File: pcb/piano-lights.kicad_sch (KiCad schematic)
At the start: 35 parts, among them J1 FTDI RS232, J2 USB_B_Micro, J3 LED Strip, J4 AVR-ISP-6, J5 MIDI IN, J6 MIDI THRU, J7 MIDI Coupler Out, J8 MIDI Coupler In, SW2 Reset, U1 ATmega328P-P, U2 H11L1, U3 74AHC1G125, Y1 16MHz

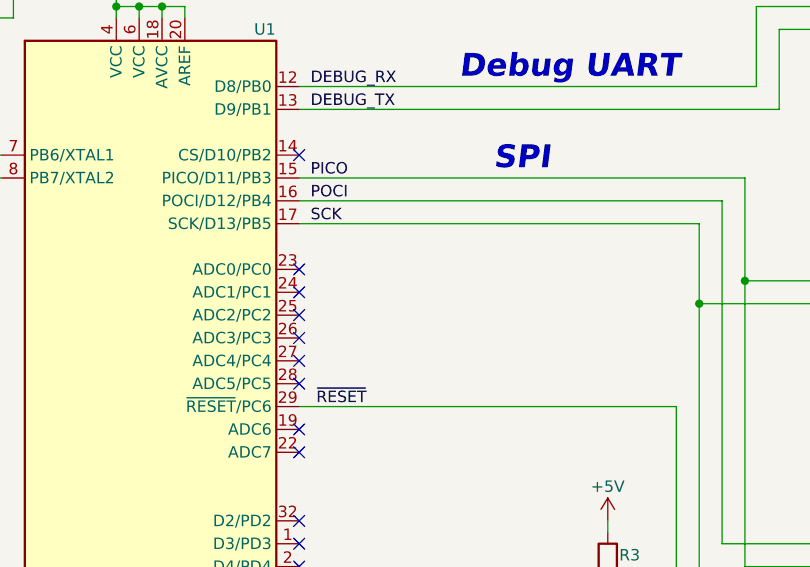
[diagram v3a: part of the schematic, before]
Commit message: Add the button back, but on a different pin. Start cleaning up silkscreen
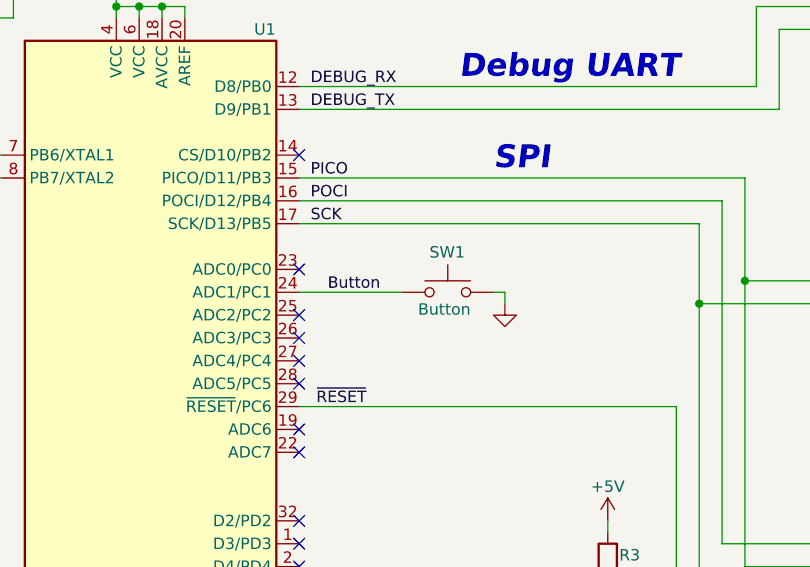
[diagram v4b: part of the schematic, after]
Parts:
- added SW1: Button, Button_Switch_THT:SW_PUSH_6mm_H5mm, symbol Switch:SW_Push
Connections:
- net GND: now also SW1.2
- net Button: now reaches U1.24 (ADC1/PC1)
- net Button: now also SW1.1
- no-connect marks 30 -> 29
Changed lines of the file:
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@@
   (no_connect (at 130.81 63.5))
   (no_connect (at 130.81 101.6))
-  (no_connect (at 130.81 66.04))
   (no_connect (at 130.81 68.58))
   (no_connect (at 130.81 71.12))
@@
     (stroke (width 0) (type default) (color 0 0 0 0))
   )
+  (wire (pts (xy 130.81 66.04) (xy 142.24 66.04))
+    (stroke (width 0) (type default) (color 0 0 0 0))
+  )
   (wire (pts (xy 44.45 50.8) (xy 45.72 50.8))
     (stroke (width 0) (type default) (color 0 0 0 0))
@@
     (stroke (width 0) (type default) (color 0 0 0 0))
   )
+  (wire (pts (xy 153.67 66.04) (xy 153.67 67.31))
+    (stroke (width 0) (type default) (color 0 0 0 0))
+  )
   (polyline (pts (xy 191.77 48.26) (xy 191.77 74.93))
     (stroke (width 0) (type default) (color 0 0 0 0))
@@
   )
   (wire (pts (xy 220.98 154.94) (xy 220.98 147.066))
+    (stroke (width 0) (type default) (color 0 0 0 0))
+  )
+  (wire (pts (xy 152.4 66.04) (xy 153.67 66.04))
     (stroke (width 0) (type default) (color 0 0 0 0))
   )
@@
   )
   (label "MCOUP_DATA" (at 232.41 157.48 0)
+    (effects (font (size 1.27 1.27)) (justify left bottom))
+  )
+  (label "Button" (at 133.985 66.04 0)
     (effects (font (size 1.27 1.27)) (justify left bottom))
   )
@@
     (pin "9")
   )
+  (symbol (lib_id "Switch:SW_Push") (at 147.32 66.04 0) (unit 1)
+    (in_bom yes) (on_board yes)
+    (property "Reference" "SW1" (id 0) (at 149.225 61.595 0)
+      (effects (font (size 1.27 1.27)) (justify right))
+    )
+    (property "Value" "Button" (id 1) (at 149.86 67.945 0)
+      (effects (font (size 1.27 1.27)) (justify right))
+    )
+    (property "Footprint" "Button_Switch_THT:SW_PUSH_6mm_H5mm" (id 2) (at 147.32 60.96 0)
+      (effects (font (size 1.27 1.27)) hide)
+    )
+    (property "Datasheet" "~" (id 3) (at 147.32 60.96 0)
+      (effects (font (size 1.27 1.27)) hide)
+    )
+    (pin "1")
+    (pin "2")
+  )
   (symbol (lib_id "power:+5V") (at 199.39 54.61 0) (unit 1)
     (in_bom yes) (on_board yes)
@@
     )
     (property "Datasheet" "" (id 3) (at 110.49 20.32 0)
+      (effects (font (size 1.27 1.27)) hide)
+    )
+    (pin "1")
+  )
+  (symbol (lib_id "power:GND") (at 153.67 67.31 0) (mirror y) (unit 1)
+    (in_bom yes) (on_board yes) (fields_autoplaced)
+    (property "Reference" "#PWR?" (id 0) (at 153.67 73.66 0)
+      (effects (font (size 1.27 1.27)) hide)
+    )
+    (property "Value" "GND" (id 1) (at 153.67 72.39 0)
+      (effects (font (size 1.27 1.27)) hide)
+    )
+    (property "Footprint" "" (id 2) (at 153.67 67.31 0)
+      (effects (font (size 1.27 1.27)) hide)
+    )
+    (property "Datasheet" "" (id 3) (at 153.67 67.31 0)
       (effects (font (size 1.27 1.27)) hide)
     )
@@
       (reference "#PWR028") (unit 1) (value "GND") (footprint "")
     )
+    (path "/a6dd2b86-9adf-4b95-abc2-e26c3254edb0"
+      (reference "#PWR?") (unit 1) (value "GND") (footprint "")
+    )
     (path "/9521ebc8-4618-4f81-a564-0a20e7137d6b"
       (reference "C1") (unit 1) (value "100n") (footprint "Capacitor_SMD:C_0603_1608Metric_Pad1.08x0.95mm_HandSolder")
@@
       (reference "R6") (unit 1) (value "220") (footprint "Resistor_SMD:R_0603_1608Metric_Pad0.98x0.95mm_HandSolder")
     )
+    (path "/3da00856-5831-42f7-ab8b-b66876dbd199"
+      (reference "SW1") (unit 1) (value "Button") (footprint "Button_Switch_THT:SW_PUSH_6mm_H5mm")
+    )
     (path "/95e292a9-d533-4e45-ad33-fbfe25b833db"

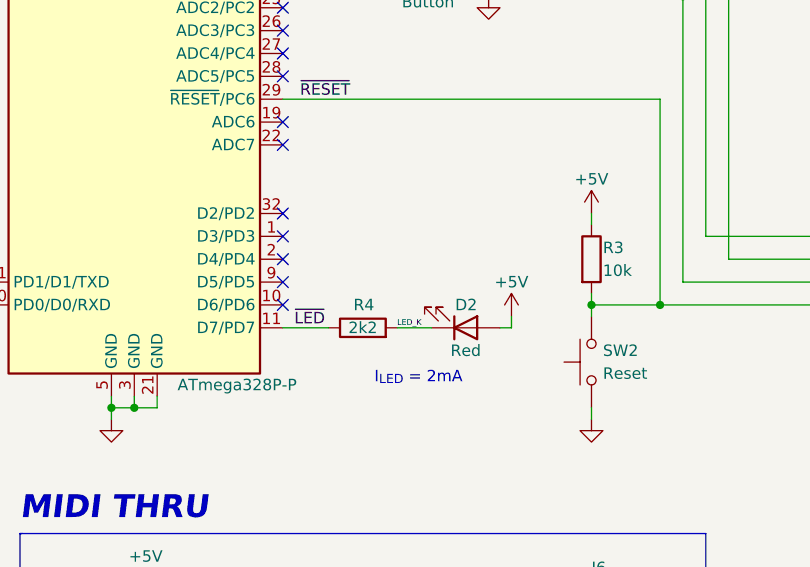
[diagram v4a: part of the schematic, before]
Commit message: Move /LED to Pin 1 for easier PCB routing
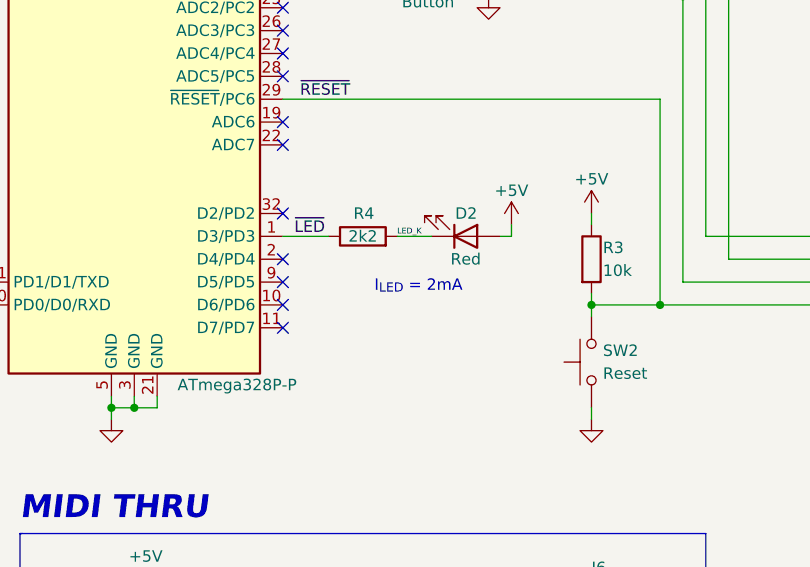
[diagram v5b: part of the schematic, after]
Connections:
- net ~{LED}: now also U1.1 (D3/PD3); no longer U1.11 (D7/PD7)
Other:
- moved on the sheet: D2, R4
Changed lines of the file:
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@@
   (no_connect (at 223.52 144.526))
   (no_connect (at 97.79 99.06))
+  (no_connect (at 130.81 104.14))
   (no_connect (at 130.81 91.44))
   (no_connect (at 130.81 81.28))
@@
   (no_connect (at 130.81 73.66))
   (no_connect (at 130.81 76.2))
-  (no_connect (at 130.81 93.98))
   (no_connect (at 130.81 96.52))
   (no_connect (at 130.81 99.06))
@@
     (stroke (width 0) (type default) (color 0 0 0 0))
   )
-  (wire (pts (xy 130.81 104.14) (xy 135.89 104.14))
+  (wire (pts (xy 130.81 93.98) (xy 135.89 93.98))
     (stroke (width 0) (type default) (color 0 0 0 0))
   )
@@
     (stroke (width 0) (type default) (color 0 0 0 0))
   )
-  (wire (pts (xy 154.94 104.14) (xy 156.21 104.14))
+  (wire (pts (xy 154.94 93.98) (xy 156.21 93.98))
     (stroke (width 0) (type default) (color 0 0 0 0))
   )
@@
     (stroke (width 0) (type default) (color 0 0 0 0))
   )
-  (wire (pts (xy 156.21 104.14) (xy 156.21 102.87))
+  (wire (pts (xy 156.21 93.98) (xy 156.21 92.71))
     (stroke (width 0) (type default) (color 0 0 0 0))
   )
@@
     (stroke (width 0) (type default) (color 0 0 0 0))
   )
-  (wire (pts (xy 143.51 104.14) (xy 147.32 104.14))
+  (wire (pts (xy 143.51 93.98) (xy 147.32 93.98))
     (stroke (width 0) (type default) (color 0 0 0 0))
   )
@@
     (effects (font (size 1.27 1.27)) (justify left bottom))
   )
-  (text "I_{LED} = 2mA" (at 140.97 110.49 0)
+  (text "I_{LED} = 2mA" (at 140.97 100.33 0)
     (effects (font (size 1.27 1.27)) (justify left bottom))
   )
@@
     (effects (font (size 1.27 1.27)) (justify right bottom))
   )
-  (label "LED_K" (at 143.51 104.14 0)
+  (label "LED_K" (at 143.51 93.98 0)
     (effects (font (size 0.635 0.635)) (justify left bottom))
   )
@@
     (effects (font (size 1.27 1.27)) (justify left bottom))
   )
-  (label "~{LED}" (at 132.08 104.14 0)
+  (label "~{LED}" (at 132.08 93.98 0)
     (effects (font (size 1.27 1.27)) (justify left bottom))
   )
@@
     (pin "1")
   )
-  (symbol (lib_id "power:+5V") (at 156.21 102.87 0) (unit 1)
-    (in_bom yes) (on_board yes)
-    (property "Reference" "#PWR017" (id 0) (at 156.21 106.68 0)
-      (effects (font (size 1.27 1.27)) hide)
-    )
-    (property "Value" "+5V" (id 1) (at 156.21 99.06 0))
-    (property "Footprint" "" (id 2) (at 156.21 102.87 0)
-      (effects (font (size 1.27 1.27)) hide)
-    )
-    (property "Datasheet" "" (id 3) (at 156.21 102.87 0)
+  (symbol (lib_id "power:+5V") (at 156.21 92.71 0) (unit 1)
+    (in_bom yes) (on_board yes)
+    (property "Reference" "#PWR017" (id 0) (at 156.21 96.52 0)
+      (effects (font (size 1.27 1.27)) hide)
+    )
+    (property "Value" "+5V" (id 1) (at 156.21 88.9 0))
+    (property "Footprint" "" (id 2) (at 156.21 92.71 0)
+      (effects (font (size 1.27 1.27)) hide)
+    )
+    (property "Datasheet" "" (id 3) (at 156.21 92.71 0)
       (effects (font (size 1.27 1.27)) hide)
     )
@@
   (symbol (lib_id "power:GND") (at 153.67 67.31 0) (mirror y) (unit 1)
     (in_bom yes) (on_board yes) (fields_autoplaced)
-    (property "Reference" "#PWR?" (id 0) (at 153.67 73.66 0)
+    (property "Reference" "#PWR0101" (id 0) (at 153.67 73.66 0)
       (effects (font (size 1.27 1.27)) hide)
     )
@@
     (pin "SH")
   )
-  (symbol (lib_id "Device:LED") (at 151.13 104.14 0) (mirror x) (unit 1)
-    (in_bom yes) (on_board yes)
-    (property "Reference" "D2" (id 0) (at 152.4 101.6 0)
+  (symbol (lib_id "Device:LED") (at 151.13 93.98 0) (mirror x) (unit 1)
+    (in_bom yes) (on_board yes)
+    (property "Reference" "D2" (id 0) (at 152.4 91.44 0)
       (effects (font (size 1.27 1.27)) (justify right))
     )
-    (property "Value" "Red" (id 1) (at 151.13 106.68 0))
-    (property "Footprint" "LED_THT:LED_D3.0mm" (id 2) (at 151.13 104.14 0)
-      (effects (font (size 1.27 1.27)) hide)
-    )
-    (property "Datasheet" "~" (id 3) (at 151.13 104.14 0)
+    (property "Value" "Red" (id 1) (at 151.13 96.52 0))
+    (property "Footprint" "LED_THT:LED_D3.0mm" (id 2) (at 151.13 93.98 0)
+      (effects (font (size 1.27 1.27)) hide)
+    )
+    (property "Datasheet" "~" (id 3) (at 151.13 93.98 0)
       (effects (font (size 1.27 1.27)) hide)
     )
@@
     )
   )
-  (symbol (lib_id "Device:R") (at 139.7 104.14 90) (unit 1)
-    (in_bom yes) (on_board yes)
-    (property "Reference" "R4" (id 0) (at 140.97 101.6 90)
+  (symbol (lib_id "Device:R") (at 139.7 93.98 90) (unit 1)
+    (in_bom yes) (on_board yes)
+    (property "Reference" "R4" (id 0) (at 140.97 91.44 90)
       (effects (font (size 1.27 1.27)) (justify left))
     )
-    (property "Value" "2k2" (id 1) (at 139.7 104.14 90))
-    (property "Footprint" "Resistor_SMD:R_0603_1608Metric_Pad0.98x0.95mm_HandSolder" (id 2) (at 139.7 105.918 90)
-      (effects (font (size 1.27 1.27)) hide)
-    )
-    (property "Datasheet" "~" (id 3) (at 139.7 104.14 0)
+    (property "Value" "2k2" (id 1) (at 139.7 93.98 90))
+    (property "Footprint" "Resistor_SMD:R_0603_1608Metric_Pad0.98x0.95mm_HandSolder" (id 2) (at 139.7 95.758 90)
+      (effects (font (size 1.27 1.27)) hide)
+    )
+    (property "Datasheet" "~" (id 3) (at 139.7 93.98 0)
       (effects (font (size 1.27 1.27)) hide)
     )
@@
     )
     (path "/a6dd2b86-9adf-4b95-abc2-e26c3254edb0"
-      (reference "#PWR?") (unit 1) (value "GND") (footprint "")
+      (reference "#PWR0101") (unit 1) (value "GND") (footprint "")
     )
     (path "/9521ebc8-4618-4f81-a564-0a20e7137d6b"

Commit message: Start adding mfr, part, and vendor to schematic
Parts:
- D2: Mfr (none) -> Würth Elektronik; Part No (none) -> 151031SS04000; Vendor (none) -> https://www.digikey.com/en/products/detail/würth-elektronik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
- J2: Mfr (none) -> Würth Elektronik; Part No (none) -> 629105150521; Vendor (none) -> https://www.digikey.com/en/products/detail/würth-elektronik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
- U2: Mrf (none) -> onsemi; Part No. (none) -> H11L1M; Vendor (none) -> https://www.digikey.com/en/products/detail/onsemi/H11L1M/28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
- U3: Mfr (none) -> Nexperia USA Inc.; Part No (none) -> 74AHC1G125GV,125; Vendor (none) -> https://www.digikey.com/en/products/detail/nexperia-usa-inc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
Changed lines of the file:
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@@
+      (effects (font (size 1.27 1.27)) hide)
+    )
+    (property "Mrf" "onsemi" (id 4) (at 67.31 101.6 0)
+      (effects (font (size 1.27 1.27)) hide)
+    )
+    (property "Part No." "H11L1M" (id 5) (at 67.31 101.6 0)
+      (effects (font (size 1.27 1.27)) hide)
+    )
+    (property "Vendor" "https://www.digikey.com/en/products/detail/onsemi/H11L1M/284866" (id 6) (at 67.31 101.6 0)
       (effects (font (size 1.27 1.27)) hide)
     )
@@
       (effects (font (size 1.27 1.27)) hide)
     )
+    (property "Mfr" "Würth Elektronik" (id 4) (at 151.13 93.98 0)
+      (effects (font (size 1.27 1.27)) hide)
+    )
+    (property "Part No" "151031SS04000" (id 5) (at 151.13 93.98 0)
+      (effects (font (size 1.27 1.27)) hide)
+    )
+    (property "Vendor" "https://www.digikey.com/en/products/detail/würth-elektronik/151031SS04000/4489979" (id 6) (at 151.13 93.98 0)
+      (effects (font (size 1.27 1.27)) hide)
+    )
     (pin "1")
     (pin "2")
@@
       (effects (font (size 1.27 1.27)) hide)
     )
+    (property "Mfr" "Nexperia USA Inc." (id 4) (at 115.57 149.86 0)
+      (effects (font (size 1.27 1.27)) hide)
+    )
+    (property "Part No" "74AHC1G125GV,125" (id 5) (at 115.57 149.86 0)
+      (effects (font (size 1.27 1.27)) hide)
+    )
+    (property "Vendor" "https://www.digikey.com/en/products/detail/nexperia-usa-inc/74AHC1G125GV-125/1229485" (id 6) (at 115.57 149.86 0)
+      (effects (font (size 1.27 1.27)) hide)
+    )
     (pin "1")
     (pin "2")
@@
       (effects (font (size 1.27 1.27)) hide)
     )
+    (property "Mfr" "Würth Elektronik" (id 4) (at 45.72 39.37 0)
+      (effects (font (size 1.27 1.27)) hide)
+    )
+    (property "Part No" "629105150521" (id 5) (at 45.72 39.37 0)
+      (effects (font (size 1.27 1.27)) hide)
+    )
+    (property "Vendor" "https://www.digikey.com/en/products/detail/würth-elektronik/629105150521/5047751" (id 6) (at 45.72 39.37 0)
+      (effects (font (size 1.27 1.27)) hide)
+    )
